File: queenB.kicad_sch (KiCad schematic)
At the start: 157 parts, among them J3 PM254-2-17-Z-8.5, J4 TC2030, J5 TC2030, J6 MEM2061-01-188-00-A, SW1 PEC12R-4120F-S0012-C143801, SW2 JS202011AQN, SW3 JS202011AQN, U1 LM3940IMP-3.3/NOPB, U3 CC2500RGPR, U4 CS3225X7R476K160NRL, U5 STM32H743IIT6, X1 S3D26.000000B20F30T, X3 S3D26.000000B20F30T

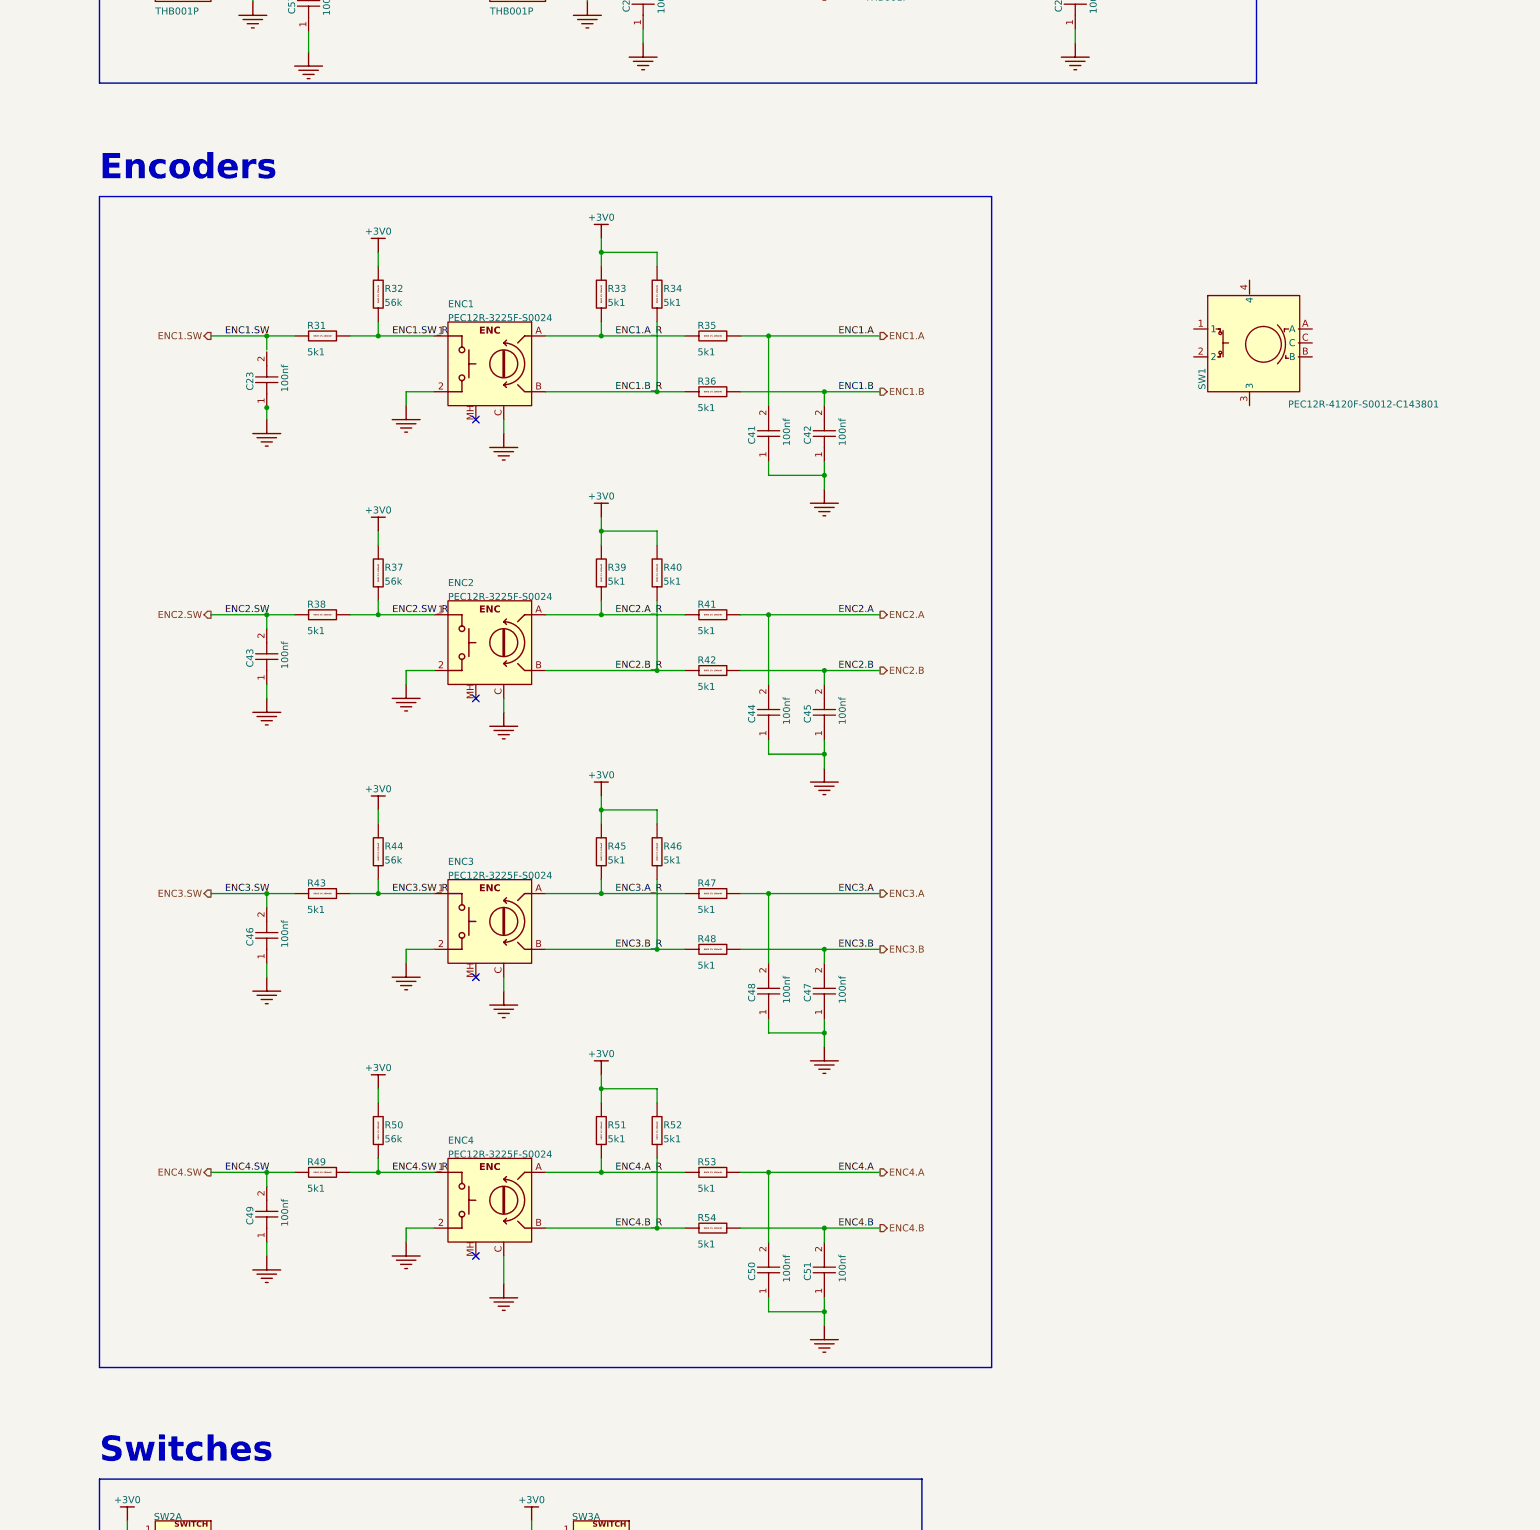
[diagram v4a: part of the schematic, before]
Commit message: Added encoder
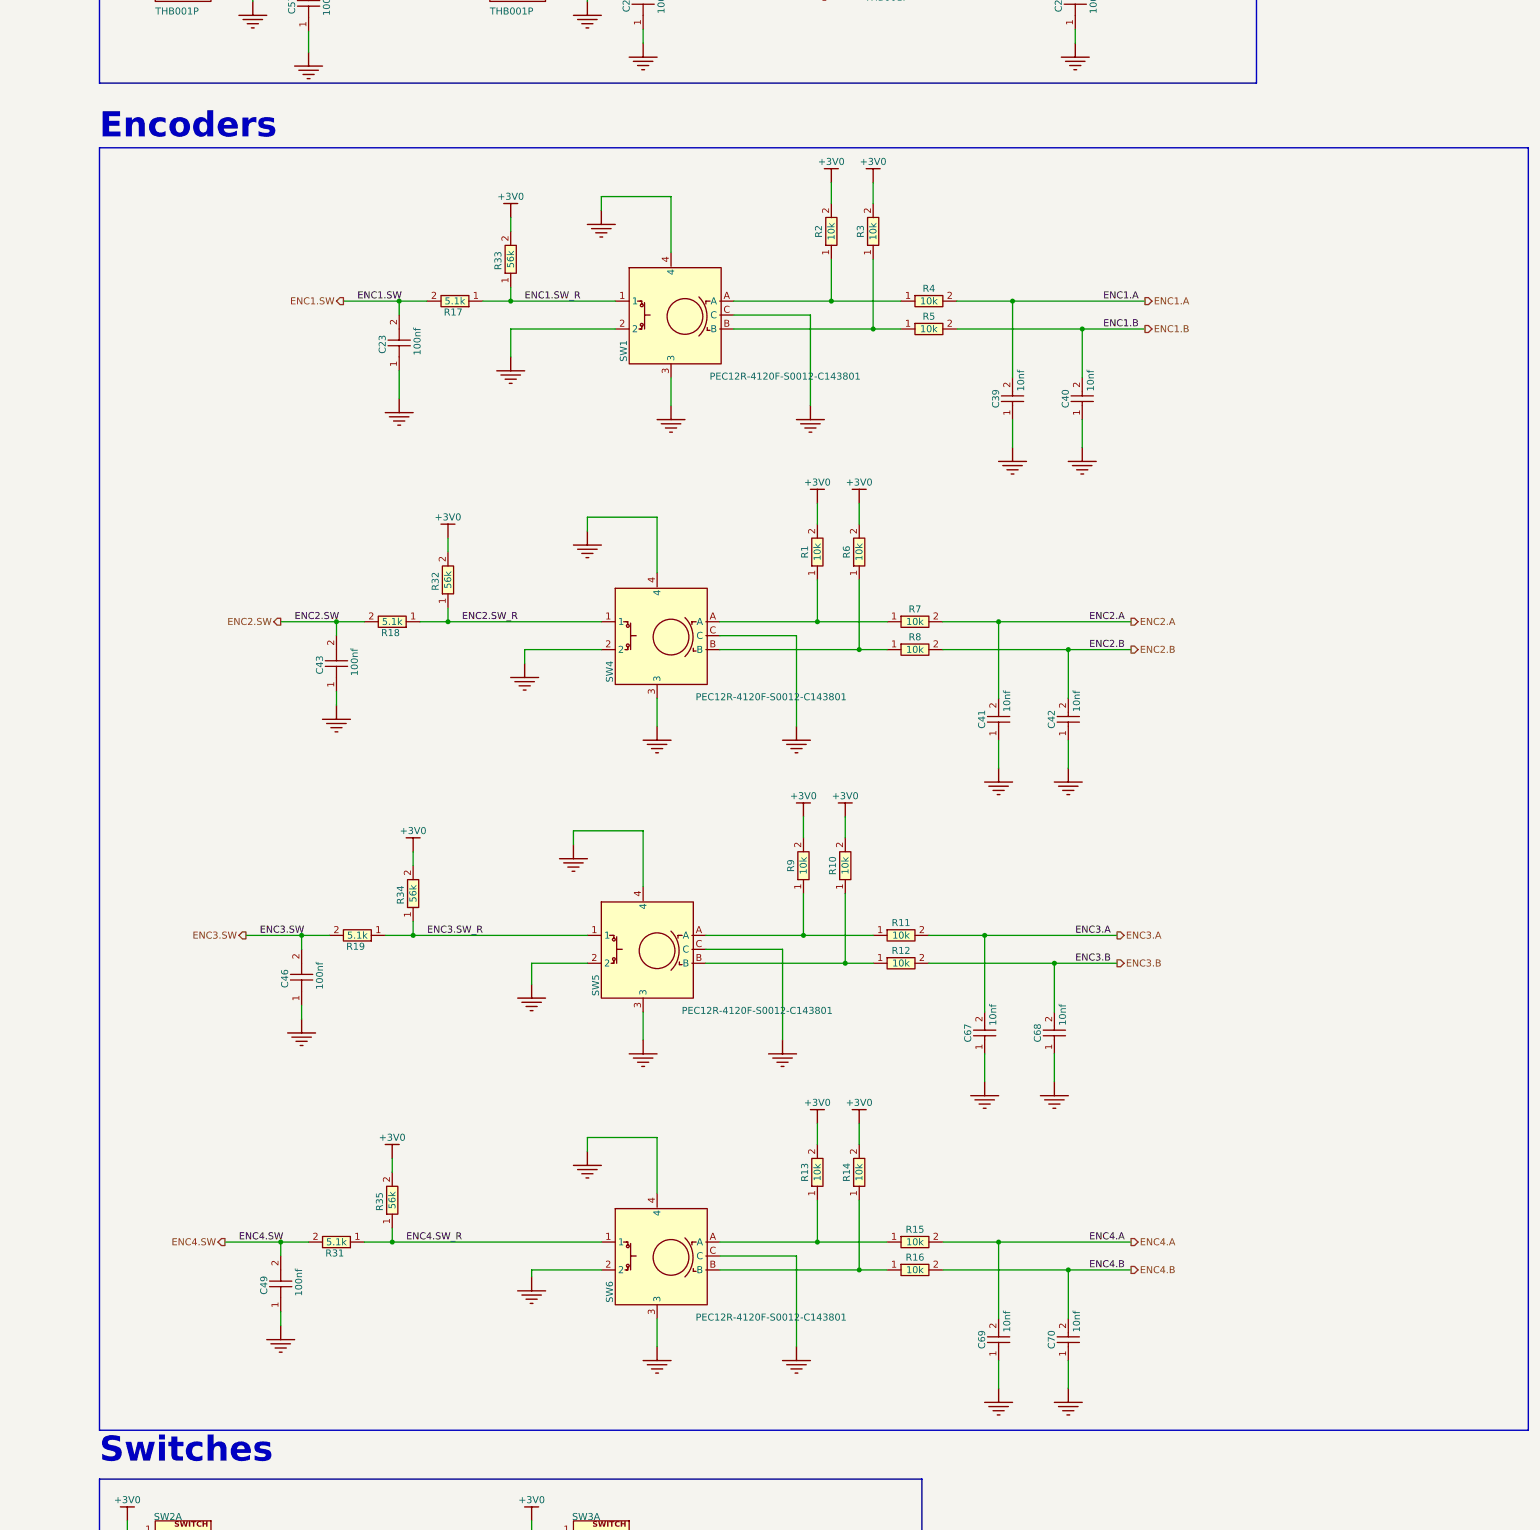
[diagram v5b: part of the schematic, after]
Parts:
- removed C41, C42, C44, C45, C47, C48, C50, C51: CC0402KRX7R7BB104, easyeda2kicad_script3:C0402, symbol easyeda2kicad_script3:CC0402KRX7R7BB104
- removed ENC1, ENC2, ENC3, ENC4: PEC12R-3225F-S0024, PhilsLab_Footprints_Control.PcbLib:PEC12R-3225F-S, symbol queenB-altium-import:root_0_PEC12R-3225F-S0024
- removed R31, R35, R36, R38, R41, R42, R43, R47, R48, R49, R53, R54: 5k1, PhilsLab_Footprints_Passive.PcbLib:RES_0603, symbol queenB-altium-import:root_0_RC0603FR-075K1L
- removed R32, R37, R44, R50: 56k, PhilsLab_Footprints_Passive.PcbLib:RES_0603, symbol queenB-altium-import:root_1_mirrored_RC0603FR-0756KL
- removed R33, R34, R39, R40, R45, R46, R51, R52: 5k1, PhilsLab_Footprints_Passive.PcbLib:RES_0603, symbol queenB-altium-import:root_1_RC0603FR-075K1L
- added C39, C40, C41, C42, C67, C68, C69, C70: CC0402KRX7R9BB103, easyeda2kicad_script:C0402, symbol easyeda2kicad_script2:CC0402KRX7R9BB103
- added R1, R10, R11, R12, R13, R14, R15, R16, R2, R3, R4, R5, R6, R7, R8, R9: 0402WGF1002TCE, easyeda2kicad_script:R0402, symbol easyeda2kicad_script2:0402WGF1002TCE
- added R17, R18, R19, R31: 0402WGF5101TCE, easyeda2kicad:R0402, symbol easyeda2kicad_script3:0402WGF5101TCE
- added R32, R33, R34, R35: 0402WGF5602TCE, easyeda2kicad:R0402, symbol easyeda2kicad_script2:0402WGF5602TCE
- added SW4, SW5, SW6: PEC12R-4120F-S0012-C143801, easyeda2kicad:SW-TH_PEC12R-4120F-S0012, symbol easyeda2kicad_script3:PEC12R-4120F-S0012-C143801
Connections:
- net +3V0: now also R1.2, R10.2, R13.2, R14.2, R2.2, R3.2, R32.2, R33.2, R34.2, R35.2, R6.2, R9.2
- net ENC1.A: now also C39.2, R4.2
- net ENC1.B: now also C40.2, R5.2
- net ENC1.SW: now also C23.2, R17.2
- net ENC1.SW_R: now also SW1.1, R17.1, R33.1
- net ENC2.A: now also C41.2, R7.2
- net ENC2.B: now also C42.2, R8.2
- net ENC2.SW: now also R18.2
- net ENC2.SW_R: now also R18.1, R32.1, SW4.1
- net ENC3.A: now also C67.2, R11.2
- net ENC3.B: now also C68.2, R12.2
- net ENC3.SW: now also R19.2
- net ENC3.SW_R: now also R19.1, R34.1, SW5.1
- net ENC4.A: now also C69.2, R15.2
- net ENC4.B: now also C70.2, R16.2
- net ENC4.SW: now also R31.2
- net ENC4.SW_R: now also R31.1, R35.1, SW6.1
- net GND: now also SW1.2, SW1.3, SW1.4, SW1.C, C39.1, C40.1, C41.1, C42.1, C67.1, C68.1, C69.1, C70.1, SW4.2, SW4.3, SW4.4, SW4.C, SW5.2, SW5.3, SW5.4, SW5.C, SW6.2, SW6.3, SW6.4, SW6.C
- net at SW1.A: now also R2.1, R4.1
- net at SW1.B: now also R3.1, R5.1
- new net: R6.1, R8.1, SW4.B
- new net: R10.1, R12.1, SW5.B
- new net: R14.1, R16.1, SW6.B
- new net: R11.1, R9.1, SW5.A
- new net: R13.1, R15.1, SW6.A
- new net: R1.1, R7.1, SW4.A
- no-connect marks 13 -> 9
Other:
- moved on the sheet: C23, C43, C46, C49, SW1
